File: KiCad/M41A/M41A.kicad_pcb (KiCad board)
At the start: 2 copper layers, 18 parts, among them SW1 RotaryEncoder_Switch, SW2 Rifle Fire, SW3 Granade fire, SW4 Cock, SW5 Magazine reload

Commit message: Actrualized KiCad project library.
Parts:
- removed H6: +5V, Connector_PinHeader_1.00mm:PinHeader_1x01_P1.00mm_Vertical
- removed H7: GND, Connector_PinHeader_1.00mm:PinHeader_1x01_P1.00mm_Vertical
- added BAT1: 5V, ProjectLibrary:BatteryLeads, F.Cu at (146.0, 89.5)
- C1: footprint Capacitor_THT:CP_Axial_L11.0mm_D5.0mm_P18.00mm_Horizontal -> Capacitor_THT:C_Disc_D3.0mm_W2.0mm_P2.50mm
- DFPlayer1: value DFR0299 -> DFPlayer
- DRV-74HC595-1: footprint Connector_PinHeader_1.00mm:PinHeader_1x03_P1.00mm_Vertical -> Connector_PinHeader_1.00mm:PinHeader_1x05_P1.00mm_Vertical
- LS1: footprint Connector_PinHeader_1.00mm:PinHeader_1x02_P1.00mm_Vertical -> ProjectLibrary:Speaker
- moved LS1 76.7 mm to (120.0, 94.5)
- moved DFPlayer1 75.9 mm to (97.9, 56.8)
- moved C1 56.0 mm to (116.0, 79.5)
- moved SW2 45.3 mm to (110.5, 53.5)
- moved SW3 45.3 mm to (110.5, 56.5)
- moved SW4 45.3 mm to (110.5, 59.5)
- moved D1-Granade1 45.3 mm to (110.5, 47.4)
- moved D2-Rifle1 45.3 mm to (110.5, 50.4)
- moved SW5 45.3 mm to (110.5, 62.6)
- moved R3 41.4 mm to (87.9, 87.2)
- moved R1 30.6 mm to (87.9, 80.8)
- moved R2 30.6 mm to (87.9, 84.0)
- moved A1 28.8 mm to (69.1, 50.4)
- moved SW1 27.3 mm to (102.0, 85.5)
- moved DRV-74HC595-1 27.3 mm to (98.7, 85.5)
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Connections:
- A1 pad 27: +5V -> Net-(A1-+5V)
- D1 pad 2: +5V -> Net-(A1-+5V)
- SW1 pad 1: Net-(A1-D9) -> (no net)
- SW1 pad 2: Net-(A1-D10) -> (no net)
- SW1 pad 3: Net-(A1-A1) -> (no net)

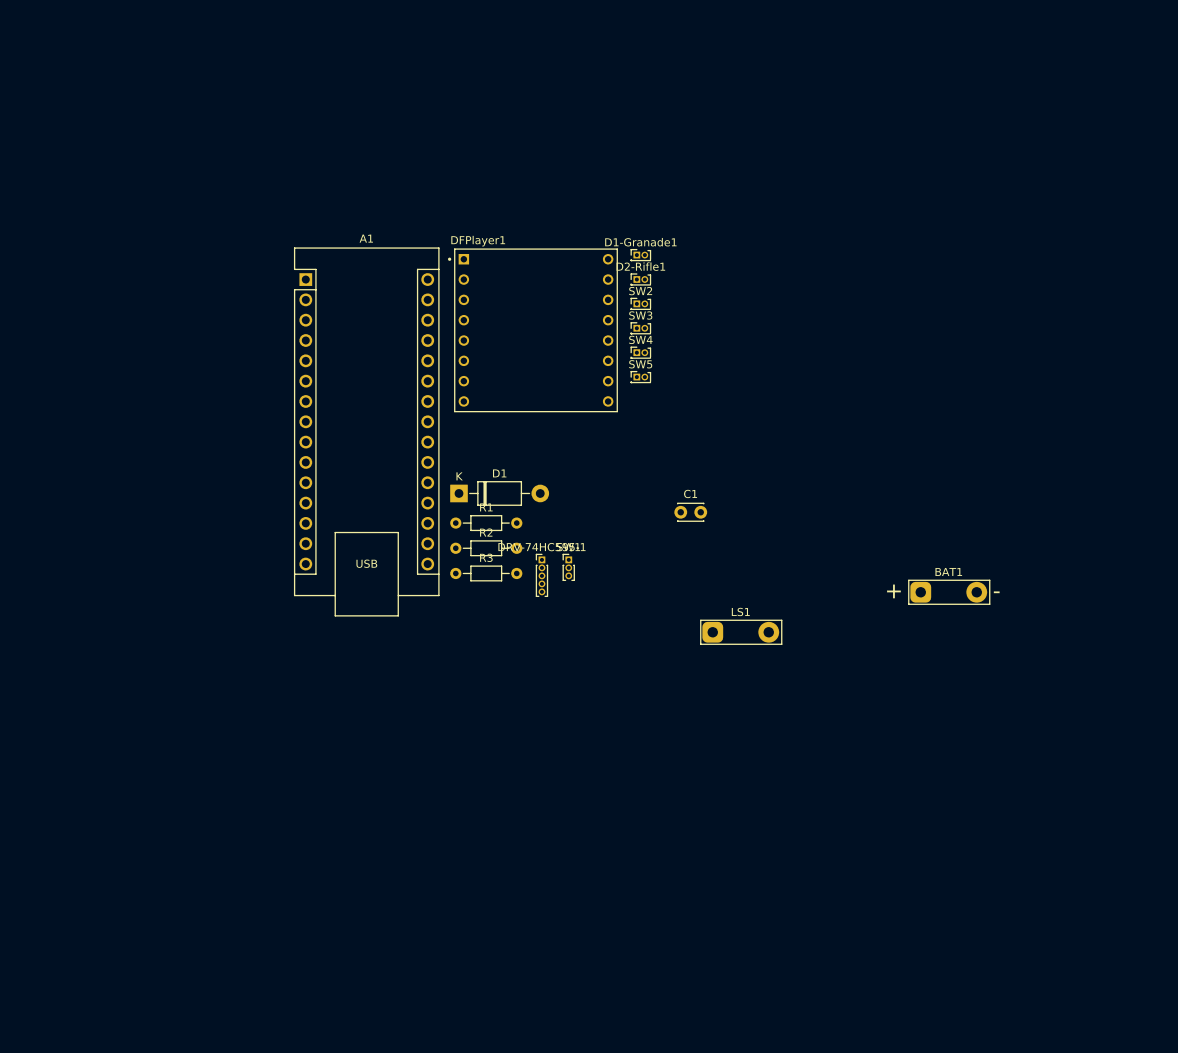
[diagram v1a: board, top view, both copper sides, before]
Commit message: Little chage in connection to key pin of rotary encoder.
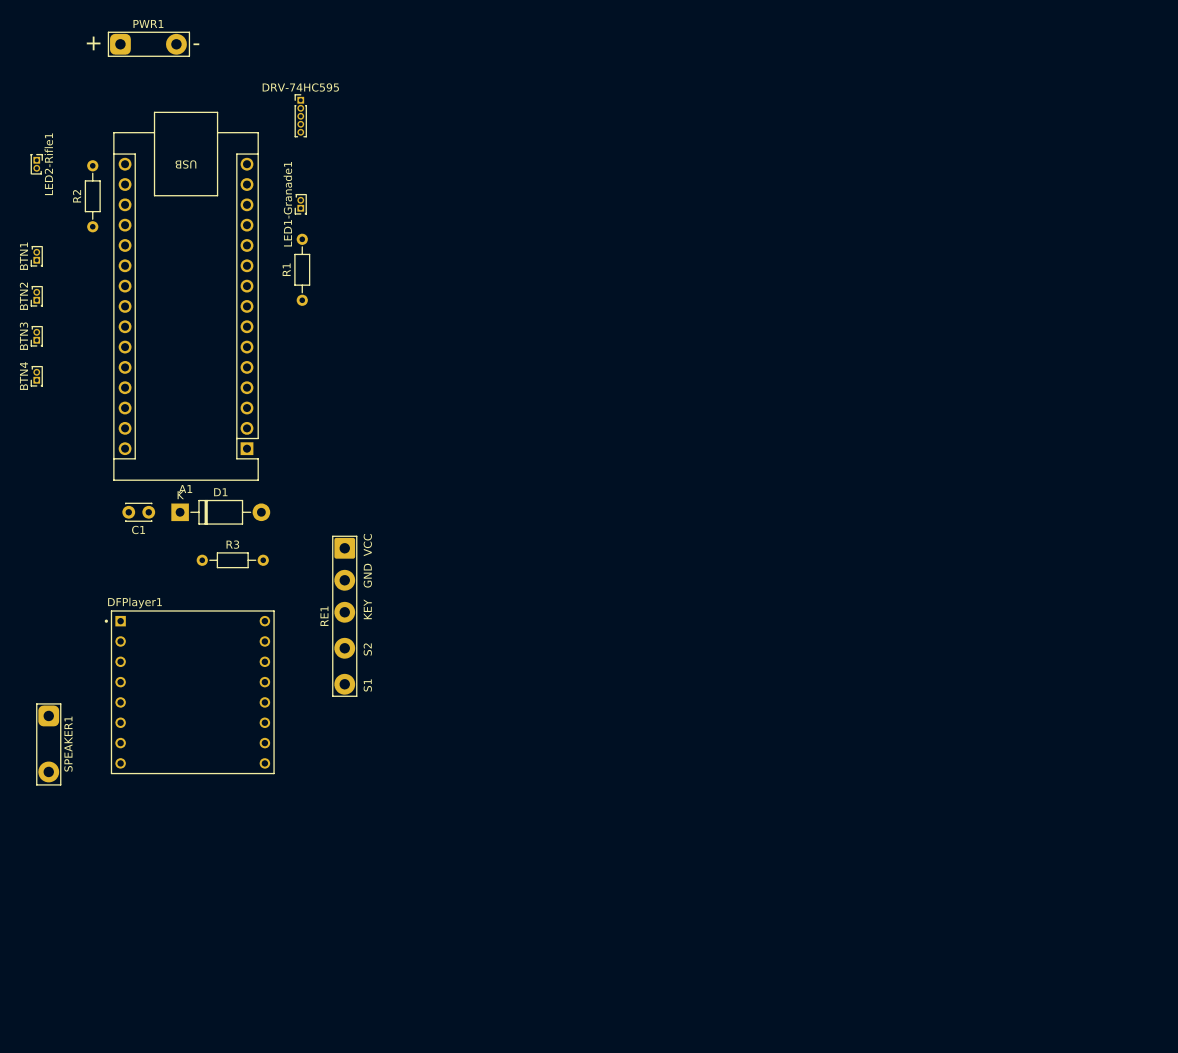
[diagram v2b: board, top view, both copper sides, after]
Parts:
- removed BAT1: 5V, ProjectLibrary:BatteryLeads
- removed D1-Granade1, D2-Rifle1: LED, Connector_PinHeader_1.00mm:PinHeader_2x01_P1.00mm_Vertical
- removed DRV-74HC595-1: ~, Connector_PinHeader_1.00mm:PinHeader_1x05_P1.00mm_Vertical
- removed LS1: Speaker 3W, ProjectLibrary:Speaker
- removed SW1: RotaryEncoder_Switch, Connector_PinHeader_1.00mm:PinHeader_1x03_P1.00mm_Vertical
- removed SW2: Rifle Fire, Connector_PinHeader_1.00mm:PinHeader_2x01_P1.00mm_Vertical
- removed SW3: Granade fire, Connector_PinHeader_1.00mm:PinHeader_2x01_P1.00mm_Vertical
- removed SW4: Cock, Connector_PinHeader_1.00mm:PinHeader_2x01_P1.00mm_Vertical
- removed SW5: Magazine reload, Connector_PinHeader_1.00mm:PinHeader_2x01_P1.00mm_Vertical
- added BTN1: Rifle Fire, Connector_PinHeader_1.00mm:PinHeader_2x01_P1.00mm_Vertical, F.Cu at (35.5, 48.0)
- added BTN2: Magazine reload, Connector_PinHeader_1.00mm:PinHeader_2x01_P1.00mm_Vertical, F.Cu at (35.5, 53.0)
- added BTN3: Cock, Connector_PinHeader_1.00mm:PinHeader_2x01_P1.00mm_Vertical, F.Cu at (35.5, 58.0)
- added BTN4: Granade fire, Connector_PinHeader_1.00mm:PinHeader_2x01_P1.00mm_Vertical, F.Cu at (35.5, 63.0)
- added DRV-74HC595: ~, Connector_PinHeader_1.00mm:PinHeader_1x05_P1.00mm_Vertical, F.Cu at (68.5, 28.0)
- added LED1-Granade1: LED, Connector_PinHeader_1.00mm:PinHeader_2x01_P1.00mm_Vertical, F.Cu at (68.5, 41.5)
- added LED2-Rifle1: LED, Connector_PinHeader_1.00mm:PinHeader_2x01_P1.00mm_Vertical, F.Cu at (35.5, 35.5)
- added PWR1: 5V, ProjectLibrary:Battery, F.Cu at (46.0, 21.0)
- added RE1: RotaryEncoder_Switch, ProjectLibrary:RotaryEncoderLeads, F.Cu at (74.0, 101.0)
- added SPEAKER1: 3W, ProjectLibrary:Speaker, F.Cu at (37.0, 105.0)
- moved C1 66.5 mm to (49.5, 79.5), turned to 180 degrees
- moved DFPlayer1 62.3 mm to (55.0, 102.0)
- moved R2 60.6 mm to (42.5, 43.8), turned to 90 degrees
- moved D1 34.9 mm to (53.4, 79.5)
- moved R1 33.8 mm to (68.7, 53.0), turned to 90 degrees
- moved R3 31.7 mm to (56.2, 85.5)
- moved A1 22.4 mm to (61.8, 71.5), turned to 180 degrees
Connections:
- A1 pad 11: unconnected-(A1-D8-Pad11) -> Net-(A1-D8)
- A1 pad 12: Net-(A1-D9) -> unconnected-(A1-D9-Pad12)
- A1 pad 13: Net-(A1-D10) -> unconnected-(A1-D10-Pad13)
- A1 pad 20: Net-(A1-A1) -> unconnected-(A1-A1-Pad20)

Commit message: +KiCad schematic files
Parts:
- added REF**: SolderWire-0.75sqmm_1x01_D1.00mm_OD2.0mm, ProjectLibrary:1x01_no_silk, F.Cu at (94.0, 38.1)
- added REF**1: SolderWire-0.75sqmm_1x01_D1.00mm_OD2.0mm, ProjectLibrary:1x01_no_silk, F.Cu at (96.5, 38.1)
- added REF**102: SolderWire-0.75sqmm_1x01_D1.00mm_OD2.0mm, ProjectLibrary:1x01_no_silk, F.Cu at (124.5, 50.8)
- added REF**103: SolderWire-0.75sqmm_1x01_D1.00mm_OD2.0mm, ProjectLibrary:1x01_no_silk, F.Cu at (127.0, 50.8)
- added REF**104: SolderWire-0.75sqmm_1x01_D1.00mm_OD2.0mm, ProjectLibrary:1x01_no_silk, F.Cu at (129.5, 50.8)
- added REF**105: SolderWire-0.75sqmm_1x01_D1.00mm_OD2.0mm, ProjectLibrary:1x01_no_silk, F.Cu at (132.1, 50.8)
- added REF**106: SolderWire-0.75sqmm_1x01_D1.00mm_OD2.0mm, ProjectLibrary:1x01_no_silk, F.Cu at (134.6, 50.8)
- added REF**107: SolderWire-0.75sqmm_1x01_D1.00mm_OD2.0mm, ProjectLibrary:1x01_no_silk, F.Cu at (137.2, 50.8)
- added REF**108: SolderWire-0.75sqmm_1x01_D1.00mm_OD2.0mm, ProjectLibrary:1x01_no_silk, F.Cu at (94.0, 53.3)
- added REF**109: SolderWire-0.75sqmm_1x01_D1.00mm_OD2.0mm, ProjectLibrary:1x01_no_silk, F.Cu at (96.5, 53.3)
- added REF**110: SolderWire-0.75sqmm_1x01_D1.00mm_OD2.0mm, ProjectLibrary:1x01_no_silk, F.Cu at (99.1, 53.3)
- added REF**111: SolderWire-0.75sqmm_1x01_D1.00mm_OD2.0mm, ProjectLibrary:1x01_no_silk, F.Cu at (101.6, 53.3)
- added REF**112: SolderWire-0.75sqmm_1x01_D1.00mm_OD2.0mm, ProjectLibrary:1x01_no_silk, F.Cu at (104.1, 53.3)
- added REF**113: SolderWire-0.75sqmm_1x01_D1.00mm_OD2.0mm, ProjectLibrary:1x01_no_silk, F.Cu at (106.7, 53.3)
- added REF**114: SolderWire-0.75sqmm_1x01_D1.00mm_OD2.0mm, ProjectLibrary:1x01_no_silk, F.Cu at (109.2, 53.3)
- added REF**12: SolderWire-0.75sqmm_1x01_D1.00mm_OD2.0mm, ProjectLibrary:1x01_no_silk, F.Cu at (124.5, 38.1)
- added REF**120: SolderWire-0.75sqmm_1x01_D1.00mm_OD2.0mm, ProjectLibrary:1x01_no_silk, F.Cu at (124.5, 53.3)
- added REF**121: SolderWire-0.75sqmm_1x01_D1.00mm_OD2.0mm, ProjectLibrary:1x01_no_silk, F.Cu at (127.0, 53.3)
- added REF**122: SolderWire-0.75sqmm_1x01_D1.00mm_OD2.0mm, ProjectLibrary:1x01_no_silk, F.Cu at (129.5, 53.3)
- added REF**123: SolderWire-0.75sqmm_1x01_D1.00mm_OD2.0mm, ProjectLibrary:1x01_no_silk, F.Cu at (132.1, 53.3)
- added REF**124: SolderWire-0.75sqmm_1x01_D1.00mm_OD2.0mm, ProjectLibrary:1x01_no_silk, F.Cu at (134.6, 53.3)
- added REF**125: SolderWire-0.75sqmm_1x01_D1.00mm_OD2.0mm, ProjectLibrary:1x01_no_silk, F.Cu at (137.2, 53.3)
- added REF**126: SolderWire-0.75sqmm_1x01_D1.00mm_OD2.0mm, ProjectLibrary:1x01_no_silk, F.Cu at (94.0, 55.9)
- added REF**127: SolderWire-0.75sqmm_1x01_D1.00mm_OD2.0mm, ProjectLibrary:1x01_no_silk, F.Cu at (96.5, 55.9)
- added REF**128: SolderWire-0.75sqmm_1x01_D1.00mm_OD2.0mm, ProjectLibrary:1x01_no_silk, F.Cu at (99.1, 55.9)
- added REF**129: SolderWire-0.75sqmm_1x01_D1.00mm_OD2.0mm, ProjectLibrary:1x01_no_silk, F.Cu at (101.6, 55.9)
- added REF**13: SolderWire-0.75sqmm_1x01_D1.00mm_OD2.0mm, ProjectLibrary:1x01_no_silk, F.Cu at (127.0, 38.1)
- added REF**130: SolderWire-0.75sqmm_1x01_D1.00mm_OD2.0mm, ProjectLibrary:1x01_no_silk, F.Cu at (104.1, 55.9)
- added REF**131: SolderWire-0.75sqmm_1x01_D1.00mm_OD2.0mm, ProjectLibrary:1x01_no_silk, F.Cu at (106.7, 55.9)
- added REF**132: SolderWire-0.75sqmm_1x01_D1.00mm_OD2.0mm, ProjectLibrary:1x01_no_silk, F.Cu at (109.2, 55.9)
- added REF**138: SolderWire-0.75sqmm_1x01_D1.00mm_OD2.0mm, ProjectLibrary:1x01_no_silk, F.Cu at (124.5, 55.9)
- added REF**139: SolderWire-0.75sqmm_1x01_D1.00mm_OD2.0mm, ProjectLibrary:1x01_no_silk, F.Cu at (127.0, 55.9)
- added REF**14: SolderWire-0.75sqmm_1x01_D1.00mm_OD2.0mm, ProjectLibrary:1x01_no_silk, F.Cu at (129.5, 38.1)
- added REF**140: SolderWire-0.75sqmm_1x01_D1.00mm_OD2.0mm, ProjectLibrary:1x01_no_silk, F.Cu at (129.5, 55.9)
- added REF**141: SolderWire-0.75sqmm_1x01_D1.00mm_OD2.0mm, ProjectLibrary:1x01_no_silk, F.Cu at (132.1, 55.9)
- added REF**142: SolderWire-0.75sqmm_1x01_D1.00mm_OD2.0mm, ProjectLibrary:1x01_no_silk, F.Cu at (134.6, 55.9)
- added REF**143: SolderWire-0.75sqmm_1x01_D1.00mm_OD2.0mm, ProjectLibrary:1x01_no_silk, F.Cu at (137.2, 55.9)
- added REF**144: SolderWire-0.75sqmm_1x01_D1.00mm_OD2.0mm, ProjectLibrary:1x01_no_silk, F.Cu at (94.0, 58.4)
- added REF**145: SolderWire-0.75sqmm_1x01_D1.00mm_OD2.0mm, ProjectLibrary:1x01_no_silk, F.Cu at (96.5, 58.4)
- added REF**146: SolderWire-0.75sqmm_1x01_D1.00mm_OD2.0mm, ProjectLibrary:1x01_no_silk, F.Cu at (99.1, 58.4)
- added REF**147: SolderWire-0.75sqmm_1x01_D1.00mm_OD2.0mm, ProjectLibrary:1x01_no_silk, F.Cu at (101.6, 58.4)
- added REF**148: SolderWire-0.75sqmm_1x01_D1.00mm_OD2.0mm, ProjectLibrary:1x01_no_silk, F.Cu at (104.1, 58.4)
- added REF**149: SolderWire-0.75sqmm_1x01_D1.00mm_OD2.0mm, ProjectLibrary:1x01_no_silk, F.Cu at (106.7, 58.4)
- added REF**15: SolderWire-0.75sqmm_1x01_D1.00mm_OD2.0mm, ProjectLibrary:1x01_no_silk, F.Cu at (132.1, 38.1)
- added REF**150: SolderWire-0.75sqmm_1x01_D1.00mm_OD2.0mm, ProjectLibrary:1x01_no_silk, F.Cu at (109.2, 58.4)
- added REF**156: SolderWire-0.75sqmm_1x01_D1.00mm_OD2.0mm, ProjectLibrary:1x01_no_silk, F.Cu at (124.5, 58.4)
- added REF**157: SolderWire-0.75sqmm_1x01_D1.00mm_OD2.0mm, ProjectLibrary:1x01_no_silk, F.Cu at (127.0, 58.4)
- added REF**158: SolderWire-0.75sqmm_1x01_D1.00mm_OD2.0mm, ProjectLibrary:1x01_no_silk, F.Cu at (129.5, 58.4)
- added REF**159: SolderWire-0.75sqmm_1x01_D1.00mm_OD2.0mm, ProjectLibrary:1x01_no_silk, F.Cu at (132.1, 58.4)
- added REF**16: SolderWire-0.75sqmm_1x01_D1.00mm_OD2.0mm, ProjectLibrary:1x01_no_silk, F.Cu at (134.6, 38.1)
- added REF**160: SolderWire-0.75sqmm_1x01_D1.00mm_OD2.0mm, ProjectLibrary:1x01_no_silk, F.Cu at (134.6, 58.4)
- added REF**161: SolderWire-0.75sqmm_1x01_D1.00mm_OD2.0mm, ProjectLibrary:1x01_no_silk, F.Cu at (137.2, 58.4)
- added REF**162: SolderWire-0.75sqmm_1x01_D1.00mm_OD2.0mm, ProjectLibrary:1x01_no_silk, F.Cu at (94.0, 61.0)
- added REF**163: SolderWire-0.75sqmm_1x01_D1.00mm_OD2.0mm, ProjectLibrary:1x01_no_silk, F.Cu at (96.5, 61.0)
- added REF**164: SolderWire-0.75sqmm_1x01_D1.00mm_OD2.0mm, ProjectLibrary:1x01_no_silk, F.Cu at (99.1, 61.0)
- added REF**165: SolderWire-0.75sqmm_1x01_D1.00mm_OD2.0mm, ProjectLibrary:1x01_no_silk, F.Cu at (101.6, 61.0)
- added REF**166: SolderWire-0.75sqmm_1x01_D1.00mm_OD2.0mm, ProjectLibrary:1x01_no_silk, F.Cu at (104.1, 61.0)
- added REF**167: SolderWire-0.75sqmm_1x01_D1.00mm_OD2.0mm, ProjectLibrary:1x01_no_silk, F.Cu at (106.7, 61.0)
- added REF**168: SolderWire-0.75sqmm_1x01_D1.00mm_OD2.0mm, ProjectLibrary:1x01_no_silk, F.Cu at (109.2, 61.0)
- added REF**17: SolderWire-0.75sqmm_1x01_D1.00mm_OD2.0mm, ProjectLibrary:1x01_no_silk, F.Cu at (137.2, 38.1)
- added REF**174: SolderWire-0.75sqmm_1x01_D1.00mm_OD2.0mm, ProjectLibrary:1x01_no_silk, F.Cu at (124.5, 61.0)
- added REF**175: SolderWire-0.75sqmm_1x01_D1.00mm_OD2.0mm, ProjectLibrary:1x01_no_silk, F.Cu at (127.0, 61.0)
- added REF**176: SolderWire-0.75sqmm_1x01_D1.00mm_OD2.0mm, ProjectLibrary:1x01_no_silk, F.Cu at (129.5, 61.0)
- added REF**177: SolderWire-0.75sqmm_1x01_D1.00mm_OD2.0mm, ProjectLibrary:1x01_no_silk, F.Cu at (132.1, 61.0)
- added REF**178: SolderWire-0.75sqmm_1x01_D1.00mm_OD2.0mm, ProjectLibrary:1x01_no_silk, F.Cu at (134.6, 61.0)
- added REF**179: SolderWire-0.75sqmm_1x01_D1.00mm_OD2.0mm, ProjectLibrary:1x01_no_silk, F.Cu at (137.2, 61.0)
- added REF**18: SolderWire-0.75sqmm_1x01_D1.00mm_OD2.0mm, ProjectLibrary:1x01_no_silk, F.Cu at (94.0, 40.6)
- added REF**180: SolderWire-0.75sqmm_1x01_D1.00mm_OD2.0mm, ProjectLibrary:1x01_no_silk, F.Cu at (94.0, 63.5)
- added REF**181: SolderWire-0.75sqmm_1x01_D1.00mm_OD2.0mm, ProjectLibrary:1x01_no_silk, F.Cu at (96.5, 63.5)
- added REF**182: SolderWire-0.75sqmm_1x01_D1.00mm_OD2.0mm, ProjectLibrary:1x01_no_silk, F.Cu at (99.1, 63.5)
- added REF**183: SolderWire-0.75sqmm_1x01_D1.00mm_OD2.0mm, ProjectLibrary:1x01_no_silk, F.Cu at (101.6, 63.5)
- added REF**184: SolderWire-0.75sqmm_1x01_D1.00mm_OD2.0mm, ProjectLibrary:1x01_no_silk, F.Cu at (104.1, 63.5)
- added REF**185: SolderWire-0.75sqmm_1x01_D1.00mm_OD2.0mm, ProjectLibrary:1x01_no_silk, F.Cu at (106.7, 63.5)
- added REF**186: SolderWire-0.75sqmm_1x01_D1.00mm_OD2.0mm, ProjectLibrary:1x01_no_silk, F.Cu at (109.2, 63.5)
- added REF**19: SolderWire-0.75sqmm_1x01_D1.00mm_OD2.0mm, ProjectLibrary:1x01_no_silk, F.Cu at (96.5, 40.6)
- added REF**192: SolderWire-0.75sqmm_1x01_D1.00mm_OD2.0mm, ProjectLibrary:1x01_no_silk, F.Cu at (124.5, 63.5)
- added REF**193: SolderWire-0.75sqmm_1x01_D1.00mm_OD2.0mm, ProjectLibrary:1x01_no_silk, F.Cu at (127.0, 63.5)
- added REF**194: SolderWire-0.75sqmm_1x01_D1.00mm_OD2.0mm, ProjectLibrary:1x01_no_silk, F.Cu at (129.5, 63.5)
- added REF**195: SolderWire-0.75sqmm_1x01_D1.00mm_OD2.0mm, ProjectLibrary:1x01_no_silk, F.Cu at (132.1, 63.5)
- added REF**196: SolderWire-0.75sqmm_1x01_D1.00mm_OD2.0mm, ProjectLibrary:1x01_no_silk, F.Cu at (134.6, 63.5)
- added REF**197: SolderWire-0.75sqmm_1x01_D1.00mm_OD2.0mm, ProjectLibrary:1x01_no_silk, F.Cu at (137.2, 63.5)
- added REF**198: SolderWire-0.75sqmm_1x01_D1.00mm_OD2.0mm, ProjectLibrary:1x01_no_silk, F.Cu at (94.0, 66.0)
- added REF**199: SolderWire-0.75sqmm_1x01_D1.00mm_OD2.0mm, ProjectLibrary:1x01_no_silk, F.Cu at (96.5, 66.0)
- added REF**2: SolderWire-0.75sqmm_1x01_D1.00mm_OD2.0mm, ProjectLibrary:1x01_no_silk, F.Cu at (99.1, 38.1)
- added REF**20: SolderWire-0.75sqmm_1x01_D1.00mm_OD2.0mm, ProjectLibrary:1x01_no_silk, F.Cu at (99.1, 40.6)
- added REF**200: SolderWire-0.75sqmm_1x01_D1.00mm_OD2.0mm, ProjectLibrary:1x01_no_silk, F.Cu at (99.1, 66.0)
- added REF**201: SolderWire-0.75sqmm_1x01_D1.00mm_OD2.0mm, ProjectLibrary:1x01_no_silk, F.Cu at (101.6, 66.0)
- added REF**202: SolderWire-0.75sqmm_1x01_D1.00mm_OD2.0mm, ProjectLibrary:1x01_no_silk, F.Cu at (104.1, 66.0)
- added REF**203: SolderWire-0.75sqmm_1x01_D1.00mm_OD2.0mm, ProjectLibrary:1x01_no_silk, F.Cu at (106.7, 66.0)
- added REF**204: SolderWire-0.75sqmm_1x01_D1.00mm_OD2.0mm, ProjectLibrary:1x01_no_silk, F.Cu at (109.2, 66.0)
- added REF**21: SolderWire-0.75sqmm_1x01_D1.00mm_OD2.0mm, ProjectLibrary:1x01_no_silk, F.Cu at (101.6, 40.6)
- added REF**210: SolderWire-0.75sqmm_1x01_D1.00mm_OD2.0mm, ProjectLibrary:1x01_no_silk, F.Cu at (124.5, 66.0)
- added REF**211: SolderWire-0.75sqmm_1x01_D1.00mm_OD2.0mm, ProjectLibrary:1x01_no_silk, F.Cu at (127.0, 66.0)
- added REF**212: SolderWire-0.75sqmm_1x01_D1.00mm_OD2.0mm, ProjectLibrary:1x01_no_silk, F.Cu at (129.5, 66.0)
- added REF**213: SolderWire-0.75sqmm_1x01_D1.00mm_OD2.0mm, ProjectLibrary:1x01_no_silk, F.Cu at (132.1, 66.0)
- added REF**214: SolderWire-0.75sqmm_1x01_D1.00mm_OD2.0mm, ProjectLibrary:1x01_no_silk, F.Cu at (134.6, 66.0)
- added REF**215: SolderWire-0.75sqmm_1x01_D1.00mm_OD2.0mm, ProjectLibrary:1x01_no_silk, F.Cu at (137.2, 66.0)
- added REF**216: SolderWire-0.75sqmm_1x01_D1.00mm_OD2.0mm, ProjectLibrary:1x01_no_silk, F.Cu at (94.0, 68.6)
- added REF**217: SolderWire-0.75sqmm_1x01_D1.00mm_OD2.0mm, ProjectLibrary:1x01_no_silk, F.Cu at (96.5, 68.6)
- added REF**218: SolderWire-0.75sqmm_1x01_D1.00mm_OD2.0mm, ProjectLibrary:1x01_no_silk, F.Cu at (99.1, 68.6)
- added REF**219: SolderWire-0.75sqmm_1x01_D1.00mm_OD2.0mm, ProjectLibrary:1x01_no_silk, F.Cu at (101.6, 68.6)
- added REF**22: SolderWire-0.75sqmm_1x01_D1.00mm_OD2.0mm, ProjectLibrary:1x01_no_silk, F.Cu at (104.1, 40.6)
- added REF**220: SolderWire-0.75sqmm_1x01_D1.00mm_OD2.0mm, ProjectLibrary:1x01_no_silk, F.Cu at (104.1, 68.6)
- added REF**221: SolderWire-0.75sqmm_1x01_D1.00mm_OD2.0mm, ProjectLibrary:1x01_no_silk, F.Cu at (106.7, 68.6)
- added REF**222: SolderWire-0.75sqmm_1x01_D1.00mm_OD2.0mm, ProjectLibrary:1x01_no_silk, F.Cu at (109.2, 68.6)
- added REF**228: SolderWire-0.75sqmm_1x01_D1.00mm_OD2.0mm, ProjectLibrary:1x01_no_silk, F.Cu at (124.5, 68.6)
- added REF**229: SolderWire-0.75sqmm_1x01_D1.00mm_OD2.0mm, ProjectLibrary:1x01_no_silk, F.Cu at (127.0, 68.6)
- added REF**23: SolderWire-0.75sqmm_1x01_D1.00mm_OD2.0mm, ProjectLibrary:1x01_no_silk, F.Cu at (106.7, 40.6)
- added REF**230: SolderWire-0.75sqmm_1x01_D1.00mm_OD2.0mm, ProjectLibrary:1x01_no_silk, F.Cu at (129.5, 68.6)
- added REF**231: SolderWire-0.75sqmm_1x01_D1.00mm_OD2.0mm, ProjectLibrary:1x01_no_silk, F.Cu at (132.1, 68.6)
- added REF**232: SolderWire-0.75sqmm_1x01_D1.00mm_OD2.0mm, ProjectLibrary:1x01_no_silk, F.Cu at (134.6, 68.6)
- added REF**233: SolderWire-0.75sqmm_1x01_D1.00mm_OD2.0mm, ProjectLibrary:1x01_no_silk, F.Cu at (137.2, 68.6)
- added REF**234: SolderWire-0.75sqmm_1x01_D1.00mm_OD2.0mm, ProjectLibrary:1x01_no_silk, F.Cu at (94.0, 71.1)
- added REF**235: SolderWire-0.75sqmm_1x01_D1.00mm_OD2.0mm, ProjectLibrary:1x01_no_silk, F.Cu at (96.5, 71.1)
- added REF**236: SolderWire-0.75sqmm_1x01_D1.00mm_OD2.0mm, ProjectLibrary:1x01_no_silk, F.Cu at (99.1, 71.1)
- added REF**237: SolderWire-0.75sqmm_1x01_D1.00mm_OD2.0mm, ProjectLibrary:1x01_no_silk, F.Cu at (101.6, 71.1)
- added REF**238: SolderWire-0.75sqmm_1x01_D1.00mm_OD2.0mm, ProjectLibrary:1x01_no_silk, F.Cu at (104.1, 71.1)
- added REF**239: SolderWire-0.75sqmm_1x01_D1.00mm_OD2.0mm, ProjectLibrary:1x01_no_silk, F.Cu at (106.7, 71.1)
- added REF**24: SolderWire-0.75sqmm_1x01_D1.00mm_OD2.0mm, ProjectLibrary:1x01_no_silk, F.Cu at (109.2, 40.6)
- added REF**240: SolderWire-0.75sqmm_1x01_D1.00mm_OD2.0mm, ProjectLibrary:1x01_no_silk, F.Cu at (109.2, 71.1)
- added REF**246: SolderWire-0.75sqmm_1x01_D1.00mm_OD2.0mm, ProjectLibrary:1x01_no_silk, F.Cu at (124.5, 71.1)
- added REF**247: SolderWire-0.75sqmm_1x01_D1.00mm_OD2.0mm, ProjectLibrary:1x01_no_silk, F.Cu at (127.0, 71.1)
- added REF**248: SolderWire-0.75sqmm_1x01_D1.00mm_OD2.0mm, ProjectLibrary:1x01_no_silk, F.Cu at (129.5, 71.1)
- added REF**249: SolderWire-0.75sqmm_1x01_D1.00mm_OD2.0mm, ProjectLibrary:1x01_no_silk, F.Cu at (132.1, 71.1)
- added REF**250: SolderWire-0.75sqmm_1x01_D1.00mm_OD2.0mm, ProjectLibrary:1x01_no_silk, F.Cu at (134.6, 71.1)
- added REF**251: SolderWire-0.75sqmm_1x01_D1.00mm_OD2.0mm, ProjectLibrary:1x01_no_silk, F.Cu at (137.2, 71.1)
- added REF**252: SolderWire-0.75sqmm_1x01_D1.00mm_OD2.0mm, ProjectLibrary:1x01_no_silk, F.Cu at (94.0, 73.7)
- added REF**253: SolderWire-0.75sqmm_1x01_D1.00mm_OD2.0mm, ProjectLibrary:1x01_no_silk, F.Cu at (96.5, 73.7)
- added REF**254: SolderWire-0.75sqmm_1x01_D1.00mm_OD2.0mm, ProjectLibrary:1x01_no_silk, F.Cu at (99.1, 73.7)
- added REF**255: SolderWire-0.75sqmm_1x01_D1.00mm_OD2.0mm, ProjectLibrary:1x01_no_silk, F.Cu at (101.6, 73.7)
- added REF**256: SolderWire-0.75sqmm_1x01_D1.00mm_OD2.0mm, ProjectLibrary:1x01_no_silk, F.Cu at (104.1, 73.7)
- added REF**257: SolderWire-0.75sqmm_1x01_D1.00mm_OD2.0mm, ProjectLibrary:1x01_no_silk, F.Cu at (106.7, 73.7)
- added REF**258: SolderWire-0.75sqmm_1x01_D1.00mm_OD2.0mm, ProjectLibrary:1x01_no_silk, F.Cu at (109.2, 73.7)
- added REF**264: SolderWire-0.75sqmm_1x01_D1.00mm_OD2.0mm, ProjectLibrary:1x01_no_silk, F.Cu at (124.5, 73.7)
- added REF**265: SolderWire-0.75sqmm_1x01_D1.00mm_OD2.0mm, ProjectLibrary:1x01_no_silk, F.Cu at (127.0, 73.7)
- added REF**266: SolderWire-0.75sqmm_1x01_D1.00mm_OD2.0mm, ProjectLibrary:1x01_no_silk, F.Cu at (129.5, 73.7)
- added REF**267: SolderWire-0.75sqmm_1x01_D1.00mm_OD2.0mm, ProjectLibrary:1x01_no_silk, F.Cu at (132.1, 73.7)
- added REF**268: SolderWire-0.75sqmm_1x01_D1.00mm_OD2.0mm, ProjectLibrary:1x01_no_silk, F.Cu at (134.6, 73.7)
- added REF**269: SolderWire-0.75sqmm_1x01_D1.00mm_OD2.0mm, ProjectLibrary:1x01_no_silk, F.Cu at (137.2, 73.7)
- added REF**270: SolderWire-0.75sqmm_1x01_D1.00mm_OD2.0mm, ProjectLibrary:1x01_no_silk, F.Cu at (94.0, 76.2)
- added REF**271: SolderWire-0.75sqmm_1x01_D1.00mm_OD2.0mm, ProjectLibrary:1x01_no_silk, F.Cu at (96.5, 76.2)
- added REF**272: SolderWire-0.75sqmm_1x01_D1.00mm_OD2.0mm, ProjectLibrary:1x01_no_silk, F.Cu at (99.1, 76.2)
- added REF**273: SolderWire-0.75sqmm_1x01_D1.00mm_OD2.0mm, ProjectLibrary:1x01_no_silk, F.Cu at (101.6, 76.2)
- added REF**274: SolderWire-0.75sqmm_1x01_D1.00mm_OD2.0mm, ProjectLibrary:1x01_no_silk, F.Cu at (104.1, 76.2)
- added REF**275: SolderWire-0.75sqmm_1x01_D1.00mm_OD2.0mm, ProjectLibrary:1x01_no_silk, F.Cu at (106.7, 76.2)
- added REF**276: SolderWire-0.75sqmm_1x01_D1.00mm_OD2.0mm, ProjectLibrary:1x01_no_silk, F.Cu at (109.2, 76.2)
- added REF**282: SolderWire-0.75sqmm_1x01_D1.00mm_OD2.0mm, ProjectLibrary:1x01_no_silk, F.Cu at (124.5, 76.2)
- added REF**283: SolderWire-0.75sqmm_1x01_D1.00mm_OD2.0mm, ProjectLibrary:1x01_no_silk, F.Cu at (127.0, 76.2)
- added REF**284: SolderWire-0.75sqmm_1x01_D1.00mm_OD2.0mm, ProjectLibrary:1x01_no_silk, F.Cu at (129.5, 76.2)
- added REF**285: SolderWire-0.75sqmm_1x01_D1.00mm_OD2.0mm, ProjectLibrary:1x01_no_silk, F.Cu at (132.1, 76.2)
- added REF**286: SolderWire-0.75sqmm_1x01_D1.00mm_OD2.0mm, ProjectLibrary:1x01_no_silk, F.Cu at (134.6, 76.2)
- added REF**287: SolderWire-0.75sqmm_1x01_D1.00mm_OD2.0mm, ProjectLibrary:1x01_no_silk, F.Cu at (137.2, 76.2)
- added REF**288: SolderWire-0.75sqmm_1x01_D1.00mm_OD2.0mm, ProjectLibrary:1x01_no_silk, F.Cu at (94.0, 78.7)
- added REF**289: SolderWire-0.75sqmm_1x01_D1.00mm_OD2.0mm, ProjectLibrary:1x01_no_silk, F.Cu at (96.5, 78.7)
- added REF**290: SolderWire-0.75sqmm_1x01_D1.00mm_OD2.0mm, ProjectLibrary:1x01_no_silk, F.Cu at (99.1, 78.7)
- added REF**291: SolderWire-0.75sqmm_1x01_D1.00mm_OD2.0mm, ProjectLibrary:1x01_no_silk, F.Cu at (101.6, 78.7)
- added REF**292: SolderWire-0.75sqmm_1x01_D1.00mm_OD2.0mm, ProjectLibrary:1x01_no_silk, F.Cu at (104.1, 78.7)
- added REF**293: SolderWire-0.75sqmm_1x01_D1.00mm_OD2.0mm, ProjectLibrary:1x01_no_silk, F.Cu at (106.7, 78.7)
- added REF**294: SolderWire-0.75sqmm_1x01_D1.00mm_OD2.0mm, ProjectLibrary:1x01_no_silk, F.Cu at (109.2, 78.7)
- added REF**295: SolderWire-0.75sqmm_1x01_D1.00mm_OD2.0mm, ProjectLibrary:1x01_no_silk, F.Cu at (111.8, 76.2)
- added REF**295: SolderWire-0.75sqmm_1x01_D1.00mm_OD2.0mm, ProjectLibrary:1x01_no_silk, F.Cu at (111.8, 78.7)
- added REF**296: SolderWire-0.75sqmm_1x01_D1.00mm_OD2.0mm, ProjectLibrary:1x01_no_silk, F.Cu at (114.3, 76.2)
- added REF**296: SolderWire-0.75sqmm_1x01_D1.00mm_OD2.0mm, ProjectLibrary:1x01_no_silk, F.Cu at (114.3, 78.7)
- added REF**297: SolderWire-0.75sqmm_1x01_D1.00mm_OD2.0mm, ProjectLibrary:1x01_no_silk, F.Cu at (116.8, 76.2)
- added REF**297: SolderWire-0.75sqmm_1x01_D1.00mm_OD2.0mm, ProjectLibrary:1x01_no_silk, F.Cu at (116.8, 78.7)
- added REF**298: SolderWire-0.75sqmm_1x01_D1.00mm_OD2.0mm, ProjectLibrary:1x01_no_silk, F.Cu at (119.4, 76.2)
- added REF**298: SolderWire-0.75sqmm_1x01_D1.00mm_OD2.0mm, ProjectLibrary:1x01_no_silk, F.Cu at (119.4, 78.7)
- added REF**299: SolderWire-0.75sqmm_1x01_D1.00mm_OD2.0mm, ProjectLibrary:1x01_no_silk, F.Cu at (121.9, 76.2)
- added REF**299: SolderWire-0.75sqmm_1x01_D1.00mm_OD2.0mm, ProjectLibrary:1x01_no_silk, F.Cu at (121.9, 78.7)
- added REF**3: SolderWire-0.75sqmm_1x01_D1.00mm_OD2.0mm, ProjectLibrary:1x01_no_silk, F.Cu at (101.6, 38.1)
- added REF**30: SolderWire-0.75sqmm_1x01_D1.00mm_OD2.0mm, ProjectLibrary:1x01_no_silk, F.Cu at (124.5, 40.6)
- added REF**300: SolderWire-0.75sqmm_1x01_D1.00mm_OD2.0mm, ProjectLibrary:1x01_no_silk, F.Cu at (124.5, 78.7)
- added REF**301: SolderWire-0.75sqmm_1x01_D1.00mm_OD2.0mm, ProjectLibrary:1x01_no_silk, F.Cu at (127.0, 78.7)
- added REF**302: SolderWire-0.75sqmm_1x01_D1.00mm_OD2.0mm, ProjectLibrary:1x01_no_silk, F.Cu at (129.5, 78.7)
- added REF**303: SolderWire-0.75sqmm_1x01_D1.00mm_OD2.0mm, ProjectLibrary:1x01_no_silk, F.Cu at (132.1, 78.7)
- added REF**304: SolderWire-0.75sqmm_1x01_D1.00mm_OD2.0mm, ProjectLibrary:1x01_no_silk, F.Cu at (134.6, 78.7)
- added REF**305: SolderWire-0.75sqmm_1x01_D1.00mm_OD2.0mm, ProjectLibrary:1x01_no_silk, F.Cu at (137.2, 78.7)
- added REF**306: SolderWire-0.75sqmm_1x01_D1.00mm_OD2.0mm, ProjectLibrary:1x01_no_silk, F.Cu at (94.0, 81.3)
- added REF**307: SolderWire-0.75sqmm_1x01_D1.00mm_OD2.0mm, ProjectLibrary:1x01_no_silk, F.Cu at (96.5, 81.3)
- added REF**308: SolderWire-0.75sqmm_1x01_D1.00mm_OD2.0mm, ProjectLibrary:1x01_no_silk, F.Cu at (99.1, 81.3)
- added REF**309: SolderWire-0.75sqmm_1x01_D1.00mm_OD2.0mm, ProjectLibrary:1x01_no_silk, F.Cu at (101.6, 81.3)
- added REF**31: SolderWire-0.75sqmm_1x01_D1.00mm_OD2.0mm, ProjectLibrary:1x01_no_silk, F.Cu at (127.0, 40.6)
- added REF**310: SolderWire-0.75sqmm_1x01_D1.00mm_OD2.0mm, ProjectLibrary:1x01_no_silk, F.Cu at (104.1, 81.3)
- added REF**311: SolderWire-0.75sqmm_1x01_D1.00mm_OD2.0mm, ProjectLibrary:1x01_no_silk, F.Cu at (106.7, 81.3)
- added REF**319: SolderWire-0.75sqmm_1x01_D1.00mm_OD2.0mm, ProjectLibrary:1x01_no_silk, F.Cu at (124.5, 81.3)
- added REF**319: SolderWire-0.75sqmm_1x01_D1.00mm_OD2.0mm, ProjectLibrary:1x01_no_silk, F.Cu at (127.0, 81.3)
- added REF**32: SolderWire-0.75sqmm_1x01_D1.00mm_OD2.0mm, ProjectLibrary:1x01_no_silk, F.Cu at (129.5, 40.6)
- added REF**320: SolderWire-0.75sqmm_1x01_D1.00mm_OD2.0mm, ProjectLibrary:1x01_no_silk, F.Cu at (129.5, 81.3)
- added REF**321: SolderWire-0.75sqmm_1x01_D1.00mm_OD2.0mm, ProjectLibrary:1x01_no_silk, F.Cu at (132.1, 81.3)
- added REF**322: SolderWire-0.75sqmm_1x01_D1.00mm_OD2.0mm, ProjectLibrary:1x01_no_silk, F.Cu at (134.6, 81.3)
- added REF**323: SolderWire-0.75sqmm_1x01_D1.00mm_OD2.0mm, ProjectLibrary:1x01_no_silk, F.Cu at (137.2, 81.3)
- added REF**324: SolderWire-0.75sqmm_1x01_D1.00mm_OD2.0mm, ProjectLibrary:1x01_no_silk, F.Cu at (94.0, 83.8)
- added REF**325: SolderWire-0.75sqmm_1x01_D1.00mm_OD2.0mm, ProjectLibrary:1x01_no_silk, F.Cu at (96.5, 83.8)
- added REF**326: SolderWire-0.75sqmm_1x01_D1.00mm_OD2.0mm, ProjectLibrary:1x01_no_silk, F.Cu at (99.1, 83.8)
- added REF**327: SolderWire-0.75sqmm_1x01_D1.00mm_OD2.0mm, ProjectLibrary:1x01_no_silk, F.Cu at (101.6, 83.8)
- added REF**328: SolderWire-0.75sqmm_1x01_D1.00mm_OD2.0mm, ProjectLibrary:1x01_no_silk, F.Cu at (104.1, 83.8)
- added REF**329: SolderWire-0.75sqmm_1x01_D1.00mm_OD2.0mm, ProjectLibrary:1x01_no_silk, F.Cu at (106.7, 83.8)
- added REF**33: SolderWire-0.75sqmm_1x01_D1.00mm_OD2.0mm, ProjectLibrary:1x01_no_silk, F.Cu at (132.1, 40.6)
- added REF**337: SolderWire-0.75sqmm_1x01_D1.00mm_OD2.0mm, ProjectLibrary:1x01_no_silk, F.Cu at (124.5, 83.8)
- added REF**337: SolderWire-0.75sqmm_1x01_D1.00mm_OD2.0mm, ProjectLibrary:1x01_no_silk, F.Cu at (127.0, 83.8)
- added REF**338: SolderWire-0.75sqmm_1x01_D1.00mm_OD2.0mm, ProjectLibrary:1x01_no_silk, F.Cu at (129.5, 83.8)
- added REF**339: SolderWire-0.75sqmm_1x01_D1.00mm_OD2.0mm, ProjectLibrary:1x01_no_silk, F.Cu at (132.1, 83.8)
- added REF**34: SolderWire-0.75sqmm_1x01_D1.00mm_OD2.0mm, ProjectLibrary:1x01_no_silk, F.Cu at (134.6, 40.6)
- added REF**340: SolderWire-0.75sqmm_1x01_D1.00mm_OD2.0mm, ProjectLibrary:1x01_no_silk, F.Cu at (134.6, 83.8)
- added REF**341: SolderWire-0.75sqmm_1x01_D1.00mm_OD2.0mm, ProjectLibrary:1x01_no_silk, F.Cu at (137.2, 83.8)
- added REF**342: SolderWire-0.75sqmm_1x01_D1.00mm_OD2.0mm, ProjectLibrary:1x01_no_silk, F.Cu at (94.0, 86.4)
- added REF**343: SolderWire-0.75sqmm_1x01_D1.00mm_OD2.0mm, ProjectLibrary:1x01_no_silk, F.Cu at (96.5, 86.4)
- added REF**344: SolderWire-0.75sqmm_1x01_D1.00mm_OD2.0mm, ProjectLibrary:1x01_no_silk, F.Cu at (99.1, 86.4)
- added REF**345: SolderWire-0.75sqmm_1x01_D1.00mm_OD2.0mm, ProjectLibrary:1x01_no_silk, F.Cu at (101.6, 86.4)
- added REF**346: SolderWire-0.75sqmm_1x01_D1.00mm_OD2.0mm, ProjectLibrary:1x01_no_silk, F.Cu at (104.1, 86.4)
- added REF**347: SolderWire-0.75sqmm_1x01_D1.00mm_OD2.0mm, ProjectLibrary:1x01_no_silk, F.Cu at (106.7, 86.4)
- added REF**35: SolderWire-0.75sqmm_1x01_D1.00mm_OD2.0mm, ProjectLibrary:1x01_no_silk, F.Cu at (137.2, 40.6)
- added REF**355: SolderWire-0.75sqmm_1x01_D1.00mm_OD2.0mm, ProjectLibrary:1x01_no_silk, F.Cu at (127.0, 86.4)
- added REF**355: SolderWire-0.75sqmm_1x01_D1.00mm_OD2.0mm, ProjectLibrary:1x01_no_silk, F.Cu at (124.5, 86.4)
- added REF**356: SolderWire-0.75sqmm_1x01_D1.00mm_OD2.0mm, ProjectLibrary:1x01_no_silk, F.Cu at (129.5, 86.4)
- added REF**357: SolderWire-0.75sqmm_1x01_D1.00mm_OD2.0mm, ProjectLibrary:1x01_no_silk, F.Cu at (132.1, 86.4)
- added REF**358: SolderWire-0.75sqmm_1x01_D1.00mm_OD2.0mm, ProjectLibrary:1x01_no_silk, F.Cu at (134.6, 86.4)
- added REF**359: SolderWire-0.75sqmm_1x01_D1.00mm_OD2.0mm, ProjectLibrary:1x01_no_silk, F.Cu at (137.2, 86.4)
- added REF**36: SolderWire-0.75sqmm_1x01_D1.00mm_OD2.0mm, ProjectLibrary:1x01_no_silk, F.Cu at (94.0, 43.2)
- added REF**360: SolderWire-0.75sqmm_1x01_D1.00mm_OD2.0mm, ProjectLibrary:1x01_no_silk, F.Cu at (94.0, 88.9)
- added REF**361: SolderWire-0.75sqmm_1x01_D1.00mm_OD2.0mm, ProjectLibrary:1x01_no_silk, F.Cu at (96.5, 88.9)
- added REF**362: SolderWire-0.75sqmm_1x01_D1.00mm_OD2.0mm, ProjectLibrary:1x01_no_silk, F.Cu at (99.1, 88.9)
- added REF**363: SolderWire-0.75sqmm_1x01_D1.00mm_OD2.0mm, ProjectLibrary:1x01_no_silk, F.Cu at (101.6, 88.9)
- added REF**364: SolderWire-0.75sqmm_1x01_D1.00mm_OD2.0mm, ProjectLibrary:1x01_no_silk, F.Cu at (104.1, 88.9)
- added REF**365: SolderWire-0.75sqmm_1x01_D1.00mm_OD2.0mm, ProjectLibrary:1x01_no_silk, F.Cu at (106.7, 88.9)
- added REF**37: SolderWire-0.75sqmm_1x01_D1.00mm_OD2.0mm, ProjectLibrary:1x01_no_silk, F.Cu at (96.5, 43.2)
- added REF**373: SolderWire-0.75sqmm_1x01_D1.00mm_OD2.0mm, ProjectLibrary:1x01_no_silk, F.Cu at (127.0, 88.9)
- added REF**373: SolderWire-0.75sqmm_1x01_D1.00mm_OD2.0mm, ProjectLibrary:1x01_no_silk, F.Cu at (124.5, 88.9)
- added REF**374: SolderWire-0.75sqmm_1x01_D1.00mm_OD2.0mm, ProjectLibrary:1x01_no_silk, F.Cu at (129.5, 88.9)
- added REF**375: SolderWire-0.75sqmm_1x01_D1.00mm_OD2.0mm, ProjectLibrary:1x01_no_silk, F.Cu at (132.1, 88.9)
- added REF**376: SolderWire-0.75sqmm_1x01_D1.00mm_OD2.0mm, ProjectLibrary:1x01_no_silk, F.Cu at (134.6, 88.9)
- added REF**377: SolderWire-0.75sqmm_1x01_D1.00mm_OD2.0mm, ProjectLibrary:1x01_no_silk, F.Cu at (137.2, 88.9)
- added REF**378: SolderWire-0.75sqmm_1x01_D1.00mm_OD2.0mm, ProjectLibrary:1x01_no_silk, F.Cu at (94.0, 91.4)
- added REF**379: SolderWire-0.75sqmm_1x01_D1.00mm_OD2.0mm, ProjectLibrary:1x01_no_silk, F.Cu at (96.5, 91.4)
- added REF**38: SolderWire-0.75sqmm_1x01_D1.00mm_OD2.0mm, ProjectLibrary:1x01_no_silk, F.Cu at (99.1, 43.2)
- added REF**380: SolderWire-0.75sqmm_1x01_D1.00mm_OD2.0mm, ProjectLibrary:1x01_no_silk, F.Cu at (99.1, 91.4)
- added REF**381: SolderWire-0.75sqmm_1x01_D1.00mm_OD2.0mm, ProjectLibrary:1x01_no_silk, F.Cu at (101.6, 91.4)
- added REF**382: SolderWire-0.75sqmm_1x01_D1.00mm_OD2.0mm, ProjectLibrary:1x01_no_silk, F.Cu at (104.1, 91.4)
- added REF**383: SolderWire-0.75sqmm_1x01_D1.00mm_OD2.0mm, ProjectLibrary:1x01_no_silk, F.Cu at (106.7, 91.4)
- added REF**39: SolderWire-0.75sqmm_1x01_D1.00mm_OD2.0mm, ProjectLibrary:1x01_no_silk, F.Cu at (101.6, 43.2)
- added REF**391: SolderWire-0.75sqmm_1x01_D1.00mm_OD2.0mm, ProjectLibrary:1x01_no_silk, F.Cu at (127.0, 91.4)
- added REF**391: SolderWire-0.75sqmm_1x01_D1.00mm_OD2.0mm, ProjectLibrary:1x01_no_silk, F.Cu at (124.5, 91.4)
- added REF**392: SolderWire-0.75sqmm_1x01_D1.00mm_OD2.0mm, ProjectLibrary:1x01_no_silk, F.Cu at (129.5, 91.4)
- added REF**393: SolderWire-0.75sqmm_1x01_D1.00mm_OD2.0mm, ProjectLibrary:1x01_no_silk, F.Cu at (132.1, 91.4)
- added REF**394: SolderWire-0.75sqmm_1x01_D1.00mm_OD2.0mm, ProjectLibrary:1x01_no_silk, F.Cu at (134.6, 91.4)
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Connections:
- A1 pad 12: unconnected-(A1-D9-Pad12) -> Net-(A1-D9)
- A1 pad 13: unconnected-(A1-D10-Pad13) -> Net-(A1-D10)
- RE1 pad 1: unconnected-(RE1-S1-Pad1) -> Net-(A1-D9)
- RE1 pad 2: unconnected-(RE1-S2-Pad2) -> Net-(A1-D10)
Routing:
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
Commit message: Actualized schema
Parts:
- added C1: 100 µF, Capacitor_THT:CP_Radial_D5.0mm_P2.50mm, F.Cu at (162.6, 30.5)
- added C2: 100 nF, Capacitor_THT:C_Rect_L4.0mm_W2.5mm_P2.50mm, F.Cu at (172.8, 45.7)
- added C4: 100 nF, Capacitor_THT:C_Rect_L4.0mm_W2.5mm_P2.50mm, F.Cu at (53.3, 66.0)
- added D2: 1N5819, Diode_THT:D_DO-41_SOD81_P10.16mm_Horizontal, F.Cu at (66.0, 71.1)
- added SW1: SW_PWR_ON_OFF, Button_Switch_THT:SW_DIP_SPSTx01_Piano_10.8x4.1mm_W7.62mm_P2.54mm, F.Cu at (129.5, 22.9)
- C3: renamed from C1; value C -> 2000 µF
- moved D1 68.2 mm to (144.8, 33.0)
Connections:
- C3 pad 1: Net-(D1-K) -> Net-(D2-K)
- D1 pad 1: Net-(D1-K) -> Net-(A1-+5V)
- D1 pad 2: Net-(A1-+5V) -> Net-(D1-A)
- DFPlayer1 pad 1: Net-(D1-K) -> Net-(D2-K)
- DRV-74HC595 pad 1: Net-(A1-D11) -> Net-(A1-+5V)
- DRV-74HC595 pad 2: Net-(A1-D12) -> GND
- DRV-74HC595 pad 4: GND -> Net-(A1-D11)
- DRV-74HC595 pad 5: Net-(A1-+5V) -> Net-(A1-D12)
- PWR1 pad 1: Net-(A1-+5V) -> Net-(PWR1-+)

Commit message: Updated scheme
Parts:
- removed REF**, REF**1, REF**102, REF**103, REF**104, REF**105, REF**106, REF**107, REF**108, REF**109, REF**110, REF**111, REF**112, REF**113, REF**114, REF**12, REF**120, REF**121, REF**122, REF**123, REF**124, REF**125, REF**126, REF**127, REF**128, REF**129, REF**13, REF**130, REF**131, REF**132, REF**138, REF**139, REF**14, REF**140, REF**141, REF**142, REF**143, REF**144, REF**145, REF**146, REF**147, REF**148, REF**149, REF**15, REF**150, REF**156, REF**157, REF**158, REF**159, REF**16, REF**160, REF**161, REF**162, REF**163, REF**164, REF**165, REF**166, REF**167, REF**168, REF**17, REF**174, REF**175, REF**176, REF**177, REF**178, REF**179, REF**18, REF**180, REF**181, REF**182, REF**183, REF**184, REF**185, REF**186, REF**19, REF**192, REF**193, REF**194, REF**195, REF**196, REF**197, REF**198, REF**199, REF**2, REF**20, REF**200, REF**201, REF**202, REF**203, REF**204, REF**21, REF**210, REF**211, REF**212, REF**213, REF**214, REF**215, REF**216, REF**217, REF**218, REF**219, REF**22, REF**220, REF**221, REF**222, REF**228, REF**229, REF**23, REF**230, REF**231, REF**232, REF**233, REF**234, REF**235, REF**236, REF**237, REF**238, REF**239, REF**24, REF**240, REF**246, REF**247, REF**248, REF**249, REF**250, REF**251, REF**252, REF**253, REF**254, REF**255, REF**256, REF**257, REF**258, REF**264, REF**265, REF**266, REF**267, REF**268, REF**269, REF**270, REF**271, REF**272, REF**273, REF**274, REF**275, REF**276, REF**282, REF**283, REF**284, REF**285, REF**286, REF**287, REF**288, REF**289, REF**290, REF**291, REF**292, REF**293, REF**294, REF**295 (x2), REF**296 (x2), REF**297 (x2), REF**298 (x2), REF**299 (x2), REF**3, REF**30, REF**300, REF**301, REF**302, REF**303, REF**304, REF**305, REF**306, REF**307, REF**308, REF**309, REF**31, REF**310, REF**311, REF**319 (x2), REF**32, REF**320, REF**321, REF**322, REF**323, REF**324, REF**325, REF**326, REF**327, REF**328, REF**329, REF**33, REF**337 (x2), REF**338, REF**339, REF**34, REF**340, REF**341, REF**342, REF**343, REF**344, REF**345, REF**346, REF**347, REF**35, REF**355 (x2), REF**356, REF**357, REF**358, REF**359, REF**36, REF**360, REF**361, REF**362, REF**363, REF**364, REF**365, REF**37, REF**373 (x2), REF**374, REF**375, REF**376, REF**377, REF**378, REF**379, REF**38, REF**380, REF**381, REF**382, REF**383, REF**39, REF**391 (x2), REF**392, REF**393, REF**394, REF**395, REF**396, REF**397, REF**398, REF**399, REF**4, REF**40, REF**400, REF**401, REF**409 (x2), REF**41, REF**410, REF**411, REF**412, REF**413, REF**414, REF**415, REF**416, REF**417, REF**418, REF**419, REF**42, REF**427 (x2), REF**428, REF**429, REF**430, REF**431, REF**432, REF**433, REF**434, REF**435, REF**436, REF**437, REF**445 (x2), REF**446, REF**447, REF**448, REF**449, REF**48, REF**49, REF**5, REF**50, REF**51, REF**52, REF**53, REF**54, REF**55, REF**56, REF**57, REF**58, REF**59, REF**6, REF**60, REF**66, REF**67, REF**68, REF**69, REF**70, REF**71, REF**72, REF**73, REF**74, REF**75, REF**76, REF**77, REF**78, REF**84, REF**85, REF**86, REF**87, REF**88, REF**89, REF**90, REF**91, REF**92, REF**93, REF**94, REF**95, REF**96: SolderWire-0.75sqmm_1x01_D1.00mm_OD2.0mm, ProjectLibrary:1x01_no_silk
- C3: footprint Capacitor_THT:C_Disc_D3.0mm_W2.0mm_P2.50mm -> Capacitor_THT:CP_Radial_D5.0mm_P2.50mm
- moved C1 74.1 mm to (134.6, 99.1), turned to -90 degrees
- moved C2 57.6 mm to (134.6, 88.9), turned to -90 degrees
- moved C4 56.4 mm to (99.1, 99.1), turned to 90 degrees
- moved RE1 50.3 mm to (129.5, 35.8)
- moved D2 32.1 mm to (96.5, 81.3), turned to 90 degrees
- moved DRV-74HC595 29.1 mm to (129.3, 25.4), turned to 180 degrees
- moved D1 23.0 mm to (142.2, 55.9)
- moved SW1 19.8 mm to (142.2, 38.1), turned to 90 degrees
- moved C3 18.3 mm to (91.4, 96.5), turned to -90 degrees
- moved LED2-Rifle1 18.2 mm to (91.7, 25.4), turned to 0 degrees
- moved SPEAKER1 16.3 mm to (91.4, 109.2)
- moved LED1-Granade1 14.4 mm to (127.0, 73.4), turned to 90 degrees
- moved BTN1 14.4 mm to (91.4, 33.3)
- moved PWR1 13.8 mm to (142.5, 25.4), turned to 180 degrees
- moved BTN4 13.0 mm to (91.4, 63.8), turned to -90 degrees
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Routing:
- net (no net): track 2.97 -> 0.00 mm
